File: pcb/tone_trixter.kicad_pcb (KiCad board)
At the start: 2 copper layers, 132 x 57 mm, 101 parts, among them J1 INA jack lead, J10 microSD DM3AT, J2 OUT jack lead, J3 DC 2.1mm lead, J4 Battery lead, J5 Enclosure bond, J6 OLED 1.3" 7-pin, J7 SW-L bypass, J8 INB jack lead, J9 SW-R tuner, SW1 PEC11R-4220F-S0024, U1 OPA1642AIDR, U2 OPA1642AIDR, U3 OPA1642AIDR, U4 Daisy Seed3

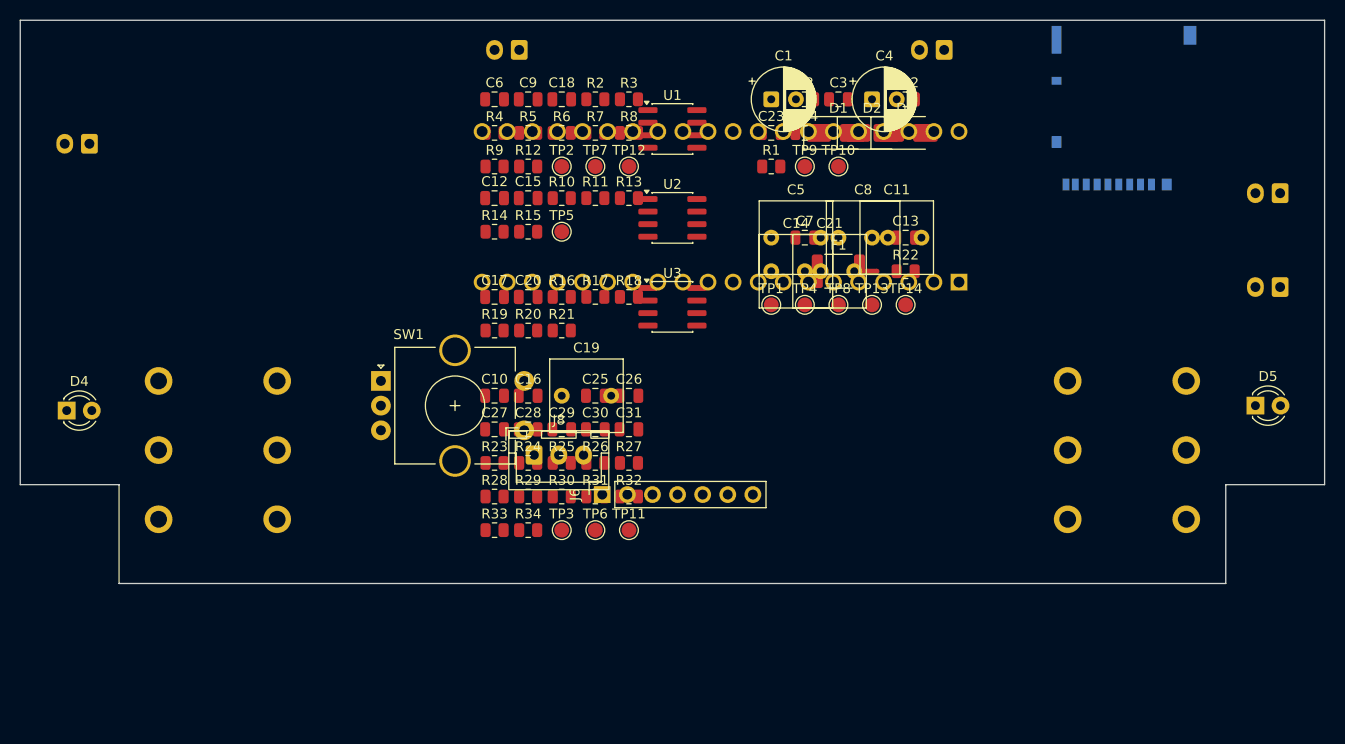
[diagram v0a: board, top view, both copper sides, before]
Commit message: pcb: restore point before left-right mirror fix
Snapshot of the current board + schematic before correcting a mirrored
placement. The 3D view (control side, player orientation) shows the
encoder/IN on the player's LEFT, but the validated paper panel template
has them on the RIGHT -- the board is a left-right mirror of the panel
(root cause: gen_place.py lacks the Y-flip gen_mockup_svg.py applies).

Includes the current hand placement, the VREF per-channel bypass caps
(C32/C33) and junction fix in gen_schematic.py. Committed as-is so the
mirror operation has a clean revert point.
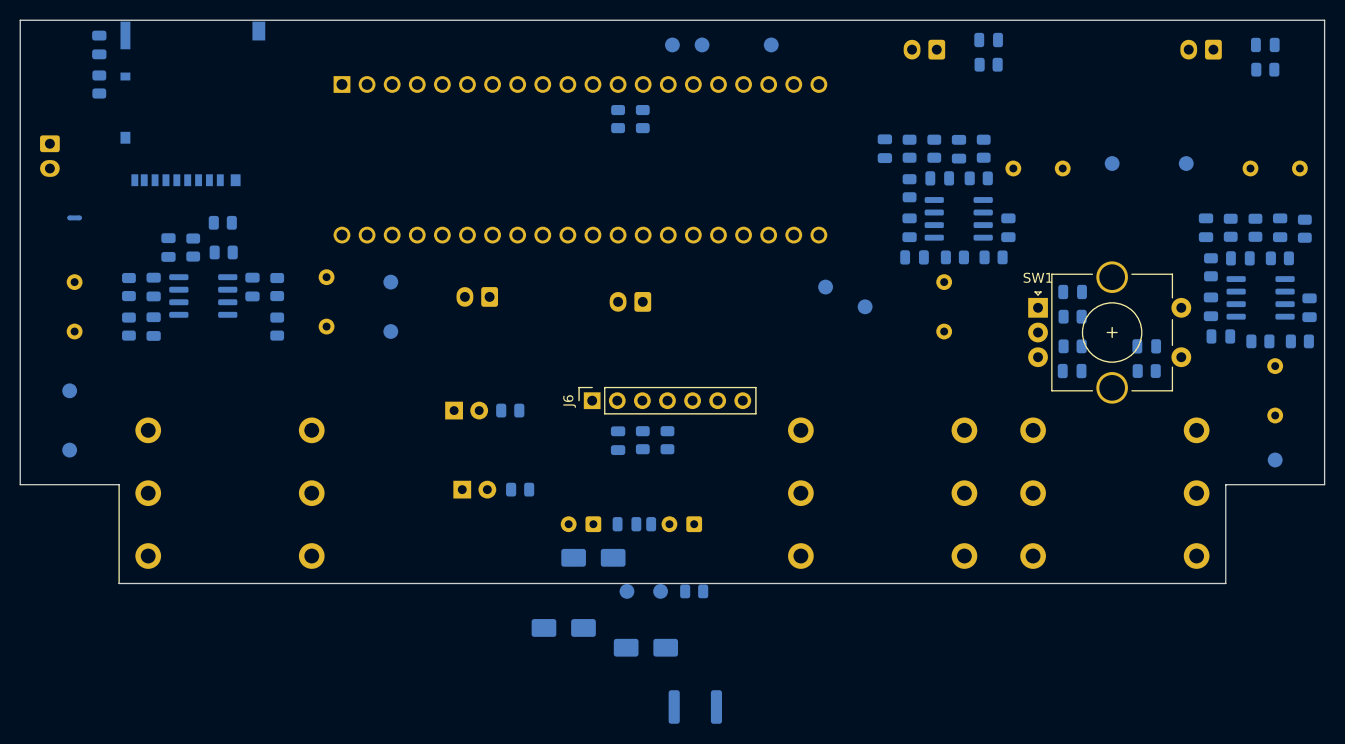
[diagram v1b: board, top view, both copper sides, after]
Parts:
- added C32: 100n, Capacitor_SMD:C_0805_2012Metric, B.Cu at (151.5, 62.0)
- added C33: 100n, Capacitor_SMD:C_0805_2012Metric, B.Cu at (120.5, 54.0)
- C1, C10, C11, C12, C13, C14, C15, C16, C17, C18, C19, C2, C20, C21, C22, C23, C24, C25, C26, C27, C28, C29, C3, C30, C31, C4, C5, C6, C7, C8, C9, D1, D2, D3, D4, D5, F1, NT1, R1, R10, R11, R12, R13, R14, R15, R16, R17, R18, R19, R2, R20, R21, R22, R23, R24, R25, R26, R27, R28, R29, R3, R30, R31, R32, R33, R34, R4, R5, R6, R7, R8, R9, TP1, TP10, TP11, TP12, TP13, TP14, TP2, TP3, TP4, TP5, TP6, TP7, TP8, TP9, U1, U2, U3: moved to B.Cu
- J8: footprint Connector_JST:JST_XH_B3B-XH-A_1x03_P2.50mm_Vertical -> TT:K3599_TRS_6leg; moved to B.Cu
- moved J10 94.2 mm to (47.5, 38.5)
- moved J1 90.9 mm to (140.8, 77.9)
- moved J2 90.9 mm to (51.2, 77.9)
- moved TP14 85.9 mm to (35.0, 73.5), turned to 180 degrees
- moved C6 85.1 mm to (160.5, 59.1), turned to -90 degrees
- moved D5 81.1 mm to (73.9, 69.5)
- moved NT1 80.9 mm to (35.5, 50.0), turned to 180 degrees
- moved R31 80.4 mm to (156.0, 35.0), turned to 180 degrees
- moved J3 80.0 mm to (77.5, 58.0)
- moved R5 79.2 mm to (160.0, 51.1), turned to 90 degrees
- moved C30 78.2 mm to (156.0, 32.5)
- moved R4 77.6 mm to (155.0, 51.0), turned to 90 degrees
- moved C10 74.0 mm to (150.0, 51.0), turned to -90 degrees
- moved R6 73.8 mm to (157.5, 54.1)
- moved C9 72.2 mm to (150.5, 59.0), turned to 90 degrees
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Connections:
- TP1 pad 1: unconnected-(TP1-Pad1) -> IN1_TIP
- TP4 pad 1: unconnected-(TP4-Pad1) -> IN2_TIP
